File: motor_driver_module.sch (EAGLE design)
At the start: 55 parts, among them IC1 LTC6088, IC7 DRV8833RTY, IC8 DRV8833RTY, P1 BAT+, P10 MD2, P11 MA_IN1, P12 MA_IN2, P13 MB_IN1, P14 MB_IN2, P15 MC_IN1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

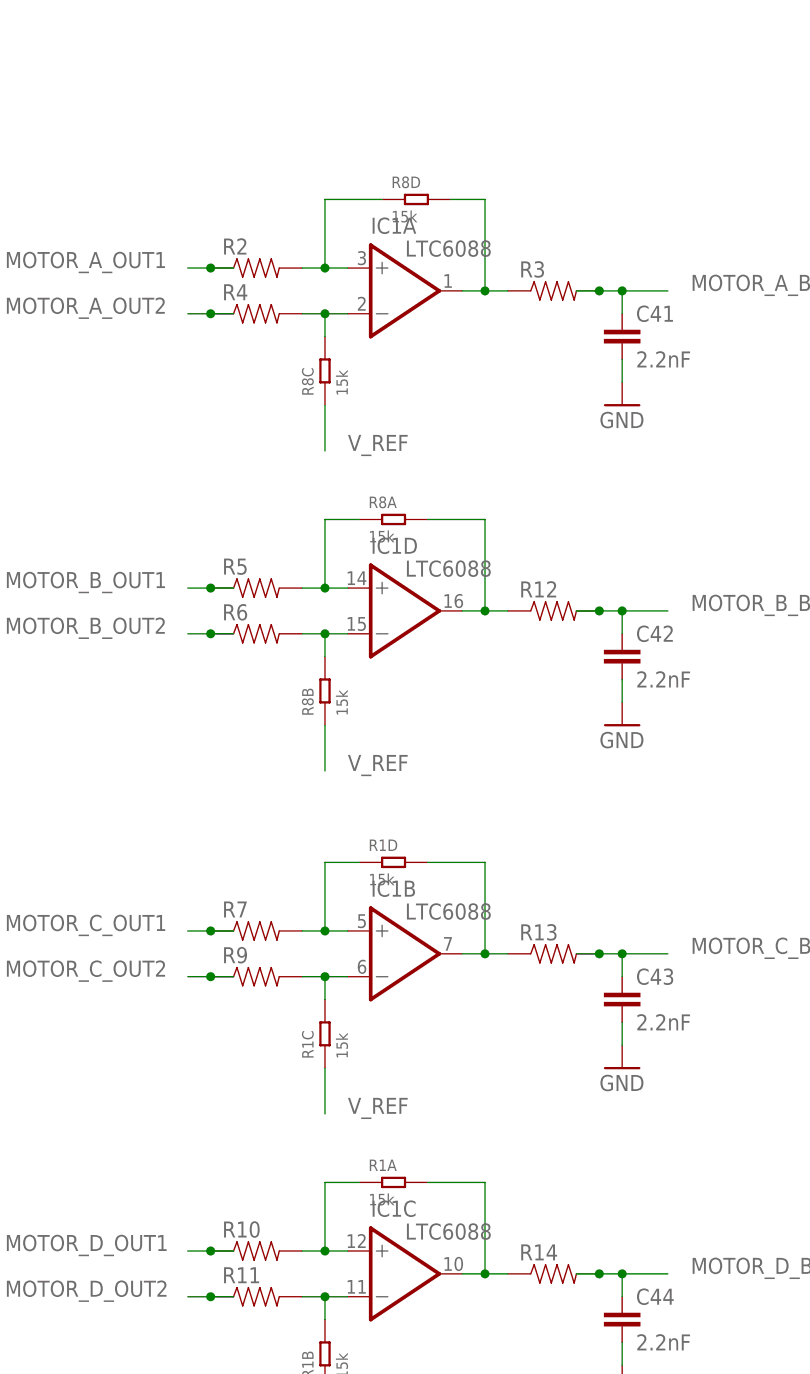
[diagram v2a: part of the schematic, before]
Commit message: More routing. No progress.
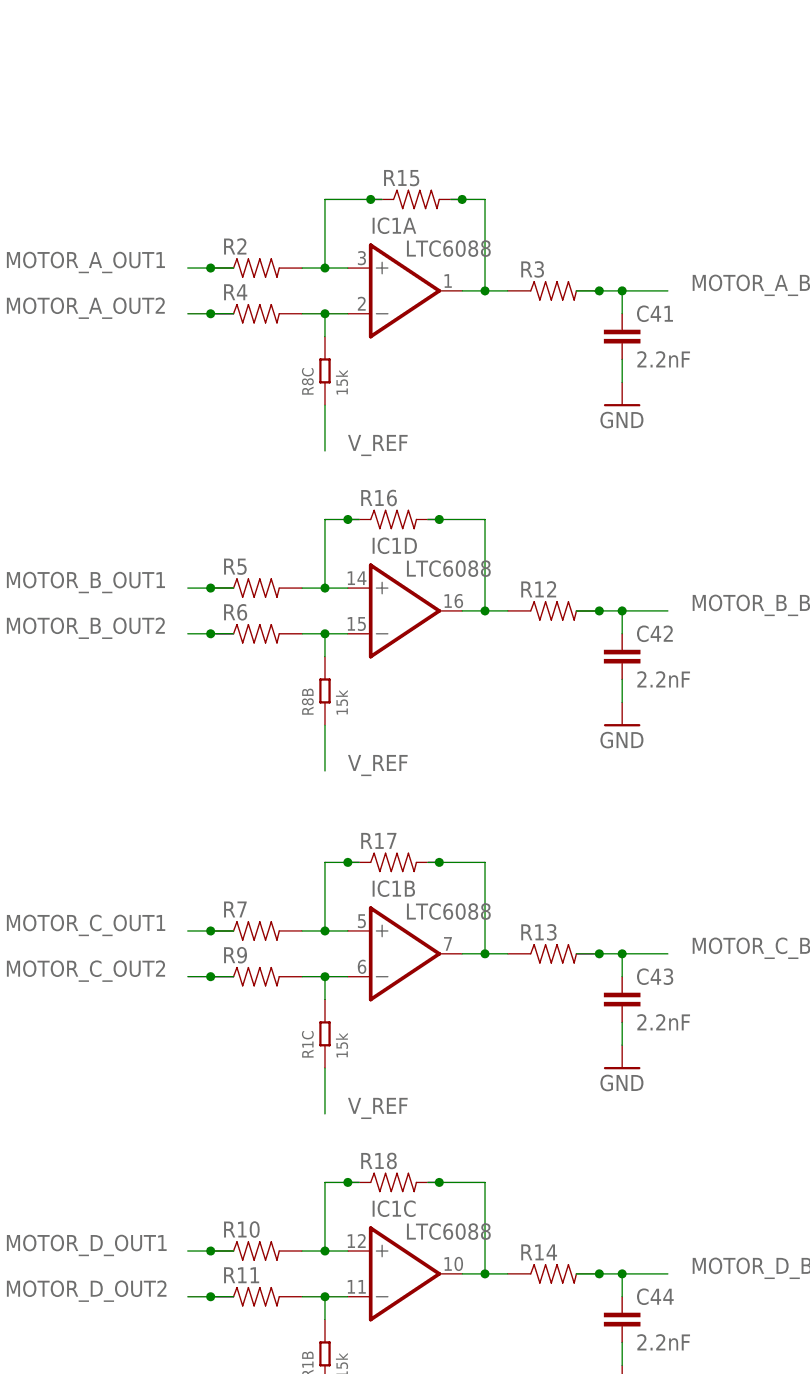
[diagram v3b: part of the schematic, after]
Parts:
- added R15, R16, R17, R18: (no value), biomimetic:RESISTOR0402-RES
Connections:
- net N$22: now also R16.1; no longer R8A.1
- net N$24: now also R17.1; no longer R1D.1
- net N$26: now also R18.1; no longer R1A.1
- net N$30: now also R15.1; no longer R8D.1
- net N$34: now also R18.2; no longer R1A.2
- net N$35: now also R17.2; no longer R1D.2
- net N$36: now also R15.2; no longer R8D.2
- net N$37: now also R16.2; no longer R8A.2
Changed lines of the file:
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@@
 <part name="R13" library="biomimetic" deviceset="RESISTOR" device="0402-RES"/>
 <part name="R14" library="biomimetic" deviceset="RESISTOR" device="0402-RES"/>
+<part name="R15" library="biomimetic" deviceset="RESISTOR" device="0402-RES"/>
+<part name="R16" library="biomimetic" deviceset="RESISTOR" device="0402-RES"/>
+<part name="R17" library="biomimetic" deviceset="RESISTOR" device="0402-RES"/>
+<part name="R18" library="biomimetic" deviceset="RESISTOR" device="0402-RES"/>
 </parts>
 <sheets>
@@
 <attribute name="VALUE" x="276.86" y="220.98" size="1.778" layer="96"/>
 </instance>
-<instance part="R1" gate="D" x="154.94" y="104.14"/>
-<instance part="R1" gate="A" x="154.94" y="68.58"/>
-<instance part="R8" gate="D" x="157.48" y="177.8"/>
-<instance part="R8" gate="A" x="154.94" y="142.24"/>
 <instance part="R8" gate="B" x="147.32" y="123.19" rot="R90"/>
 <instance part="R1" gate="C" x="147.32" y="85.09" rot="R90"/>
@@
 <instance part="R13" gate="G$1" x="172.72" y="93.98"/>
 <instance part="R14" gate="G$1" x="172.72" y="58.42"/>
+<instance part="R15" gate="G$1" x="157.48" y="177.8"/>
+<instance part="R16" gate="G$1" x="154.94" y="142.24"/>
+<instance part="R17" gate="G$1" x="154.94" y="104.14"/>
+<instance part="R18" gate="G$1" x="154.94" y="68.58"/>
 </instances>
 <busses>
@@
 <wire x1="144.78" y1="170.18" x2="147.32" y2="170.18" width="0.1524" layer="91"/>
 <wire x1="147.32" y1="170.18" x2="147.32" y2="177.8" width="0.1524" layer="91"/>
-<wire x1="147.32" y1="177.8" x2="153.67" y2="177.8" width="0.1524" layer="91"/>
+<wire x1="147.32" y1="177.8" x2="152.4" y2="177.8" width="0.1524" layer="91"/>
+<wire x1="152.4" y1="177.8" x2="153.67" y2="177.8" width="0.1524" layer="91"/>
 <wire x1="149.86" y1="170.18" x2="147.32" y2="170.18" width="0.1524" layer="91"/>
 <junction x="147.32" y="170.18"/>
-<pinref part="R8" gate="D" pin="1"/>
 <pinref part="IC1" gate="A" pin="+IN"/>
 <pinref part="R2" gate="G$1" pin="2"/>
+<pinref part="R15" gate="G$1" pin="1"/>
+<junction x="152.4" y="177.8"/>
 </segment>
 </net>
@@
 <segment>
 <wire x1="147.32" y1="134.62" x2="147.32" y2="142.24" width="0.1524" layer="91"/>
-<wire x1="147.32" y1="142.24" x2="151.13" y2="142.24" width="0.1524" layer="91"/>
+<wire x1="147.32" y1="142.24" x2="149.86" y2="142.24" width="0.1524" layer="91"/>
+<wire x1="149.86" y1="142.24" x2="151.13" y2="142.24" width="0.1524" layer="91"/>
 <wire x1="149.86" y1="134.62" x2="147.32" y2="134.62" width="0.1524" layer="91"/>
 <wire x1="144.78" y1="134.62" x2="147.32" y2="134.62" width="0.1524" layer="91"/>
 <junction x="147.32" y="134.62"/>
-<pinref part="R8" gate="A" pin="1"/>
 <pinref part="IC1" gate="D" pin="+IN"/>
 <pinref part="R5" gate="G$1" pin="2"/>
+<pinref part="R16" gate="G$1" pin="1"/>
+<junction x="149.86" y="142.24"/>
 </segment>
 </net>
@@
 <wire x1="144.78" y1="96.52" x2="147.32" y2="96.52" width="0.1524" layer="91"/>
 <wire x1="147.32" y1="96.52" x2="147.32" y2="104.14" width="0.1524" layer="91"/>
-<wire x1="147.32" y1="104.14" x2="151.13" y2="104.14" width="0.1524" layer="91"/>
+<wire x1="147.32" y1="104.14" x2="149.86" y2="104.14" width="0.1524" layer="91"/>
+<wire x1="149.86" y1="104.14" x2="151.13" y2="104.14" width="0.1524" layer="91"/>
 <wire x1="149.86" y1="96.52" x2="147.32" y2="96.52" width="0.1524" layer="91"/>
 <junction x="147.32" y="96.52"/>
-<pinref part="R1" gate="D" pin="1"/>
 <pinref part="IC1" gate="B" pin="+IN"/>
 <pinref part="R7" gate="G$1" pin="2"/>
+<pinref part="R17" gate="G$1" pin="1"/>
+<junction x="149.86" y="104.14"/>
 </segment>
 </net>
@@
 <wire x1="144.78" y1="60.96" x2="147.32" y2="60.96" width="0.1524" layer="91"/>
 <wire x1="147.32" y1="60.96" x2="147.32" y2="68.58" width="0.1524" layer="91"/>
-<wire x1="147.32" y1="68.58" x2="151.13" y2="68.58" width="0.1524" layer="91"/>
+<wire x1="147.32" y1="68.58" x2="149.86" y2="68.58" width="0.1524" layer="91"/>
+<wire x1="149.86" y1="68.58" x2="151.13" y2="68.58" width="0.1524" layer="91"/>
 <wire x1="149.86" y1="60.96" x2="147.32" y2="60.96" width="0.1524" layer="91"/>
 <junction x="147.32" y="60.96"/>
-<pinref part="R1" gate="A" pin="1"/>
 <pinref part="IC1" gate="C" pin="+IN"/>
 <pinref part="R10" gate="G$1" pin="2"/>
+<pinref part="R18" gate="G$1" pin="1"/>
+<junction x="149.86" y="68.58"/>
 </segment>
 </net>
@@
 <segment>
 <wire x1="162.56" y1="58.42" x2="165.1" y2="58.42" width="0.1524" layer="91"/>
-<wire x1="158.75" y1="68.58" x2="165.1" y2="68.58" width="0.1524" layer="91"/>
+<wire x1="158.75" y1="68.58" x2="160.02" y2="68.58" width="0.1524" layer="91"/>
+<wire x1="160.02" y1="68.58" x2="165.1" y2="68.58" width="0.1524" layer="91"/>
 <wire x1="165.1" y1="68.58" x2="165.1" y2="58.42" width="0.1524" layer="91"/>
-<pinref part="R1" gate="A" pin="2"/>
 <wire x1="165.1" y1="58.42" x2="167.64" y2="58.42" width="0.1524" layer="91"/>
 <junction x="165.1" y="58.42"/>
 <pinref part="IC1" gate="C" pin="OUT"/>
 <pinref part="R14" gate="G$1" pin="1"/>
+<pinref part="R18" gate="G$1" pin="2"/>
+<junction x="160.02" y="68.58"/>
 </segment>
 </net>
@@
 <segment>
 <wire x1="162.56" y1="93.98" x2="165.1" y2="93.98" width="0.1524" layer="91"/>
-<wire x1="158.75" y1="104.14" x2="165.1" y2="104.14" width="0.1524" layer="91"/>
+<wire x1="158.75" y1="104.14" x2="160.02" y2="104.14" width="0.1524" layer="91"/>
+<wire x1="160.02" y1="104.14" x2="165.1" y2="104.14" width="0.1524" layer="91"/>
 <wire x1="165.1" y1="104.14" x2="165.1" y2="93.98" width="0.1524" layer="91"/>
-<pinref part="R1" gate="D" pin="2"/>
 <wire x1="165.1" y1="93.98" x2="167.64" y2="93.98" width="0.1524" layer="91"/>
 <junction x="165.1" y="93.98"/>
 <pinref part="IC1" gate="B" pin="OUT"/>
 <pinref part="R13" gate="G$1" pin="1"/>
+<pinref part="R17" gate="G$1" pin="2"/>
+<junction x="160.02" y="104.14"/>
 </segment>
 </net>
@@
 <segment>
 <wire x1="162.56" y1="132.08" x2="165.1" y2="132.08" width="0.1524" layer="91"/>
-<wire x1="158.75" y1="142.24" x2="165.1" y2="142.24" width="0.1524" layer="91"/>
+<wire x1="158.75" y1="142.24" x2="160.02" y2="142.24" width="0.1524" layer="91"/>
+<wire x1="160.02" y1="142.24" x2="165.1" y2="142.24" width="0.1524" layer="91"/>
 <wire x1="165.1" y1="142.24" x2="165.1" y2="132.08" width="0.1524" layer="91"/>
-<pinref part="R8" gate="A" pin="2"/>
 <wire x1="165.1" y1="132.08" x2="167.64" y2="132.08" width="0.1524" layer="91"/>
 <junction x="165.1" y="132.08"/>
 <pinref part="IC1" gate="D" pin="OUT"/>
 <pinref part="R12" gate="G$1" pin="1"/>
+<pinref part="R16" gate="G$1" pin="2"/>
+<junction x="160.02" y="142.24"/>
 </segment>
 </net>
@@
 <segment>
 <wire x1="162.56" y1="167.64" x2="165.1" y2="167.64" width="0.1524" layer="91"/>
-<wire x1="161.29" y1="177.8" x2="165.1" y2="177.8" width="0.1524" layer="91"/>
+<wire x1="161.29" y1="177.8" x2="162.56" y2="177.8" width="0.1524" layer="91"/>
+<wire x1="162.56" y1="177.8" x2="165.1" y2="177.8" width="0.1524" layer="91"/>
 <wire x1="165.1" y1="177.8" x2="165.1" y2="167.64" width="0.1524" layer="91"/>
-<pinref part="R8" gate="D" pin="2"/>
 <wire x1="165.1" y1="167.64" x2="167.64" y2="167.64" width="0.1524" layer="91"/>
 <junction x="165.1" y="167.64"/>
 <pinref part="IC1" gate="A" pin="OUT"/>
 <pinref part="R3" gate="G$1" pin="1"/>
-</segment>
-</net>
+<pinref part="R15" gate="G$1" pin="2"/>
+<junction x="162.56" y="177.8"/>
+</segment>
+</net>

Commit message: Further routing. No progress.
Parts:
- added R19, R20: (no value), biomimetic:RESISTOR0402-RES
- R1, R8: value 15k -> (none); device OPL Eagle Library:R-4R -> biomimetic:RESISTOR0402-RES
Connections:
- net N$22: now also IC1A.+IN; no longer IC1D.+IN
- net N$23: now also IC1A.-IN, R8.2; no longer IC1D.-IN, R8B.2
- net N$25: now also R19.2; no longer R1C.2
- net N$27: now also R20.2; no longer R1B.2
- net N$30: now also IC1D.+IN; no longer IC1A.+IN
- net N$31: now also IC1D.-IN, R1.2; no longer IC1A.-IN, R8C.2
- net N$36: now also IC1D.OUT; no longer IC1A.OUT
- net N$37: now also IC1A.OUT; no longer IC1D.OUT
- net V_REF: now also R1.1, R19.1, R20.1, R8.1; no longer R1B.1, R1C.1, R8B.1, R8C.1
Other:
- moved on the sheet: IC1A, IC1D
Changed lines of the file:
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@@
 <part name="GND33" library="biomimetic" deviceset="GND" device=""/>
 <part name="GND46" library="biomimetic" deviceset="GND" device=""/>
-<part name="R8" library="OPL Eagle Library" deviceset="R-4R*" device="" value="15k"/>
 <part name="C47" library="biomimetic" deviceset="CAP" device="0402-CAP" value="0.1uF"/>
 <part name="U$1" library="biomimetic" deviceset="3.3V" device=""/>
@@
 <part name="P21" library="wirepad" deviceset="SMD2" device="" value="MOTOR_C_BEMF"/>
 <part name="P22" library="wirepad" deviceset="SMD2" device="" value="MOTOR_D_BEMF"/>
-<part name="R1" library="OPL Eagle Library" deviceset="R-4R*" device="" value="15k"/>
 <part name="IC1" library="biomimetic" deviceset="LTC6088" device=""/>
 <part name="R2" library="biomimetic" deviceset="RESISTOR" device="0402-RES"/>
@@
 <part name="R17" library="biomimetic" deviceset="RESISTOR" device="0402-RES"/>
 <part name="R18" library="biomimetic" deviceset="RESISTOR" device="0402-RES"/>
+<part name="R1" library="biomimetic" deviceset="RESISTOR" device="0402-RES"/>
+<part name="R8" library="biomimetic" deviceset="RESISTOR" device="0402-RES"/>
+<part name="R19" library="biomimetic" deviceset="RESISTOR" device="0402-RES"/>
+<part name="R20" library="biomimetic" deviceset="RESISTOR" device="0402-RES"/>
 </parts>
 <sheets>
@@
 <instance part="U$1" gate="G$1" x="111.76" y="30.48"/>
 <instance part="GND24" gate="1" x="111.76" y="7.62"/>
-<instance part="R8" gate="C" x="147.32" y="158.75" rot="R90"/>
 <instance part="P3" gate="1" x="304.8" y="160.02" smashed="yes">
 <attribute name="NAME" x="289.56" y="160.02" size="1.778" layer="95"/>
@@
 <attribute name="VALUE" x="276.86" y="220.98" size="1.778" layer="96"/>
 </instance>
-<instance part="R8" gate="B" x="147.32" y="123.19" rot="R90"/>
-<instance part="R1" gate="C" x="147.32" y="85.09" rot="R90"/>
-<instance part="R1" gate="B" x="147.32" y="49.53" rot="R90"/>
-<instance part="IC1" gate="A" x="154.94" y="167.64"/>
 <instance part="IC1" gate="B" x="154.94" y="93.98"/>
 <instance part="IC1" gate="C" x="154.94" y="58.42"/>
-<instance part="IC1" gate="D" x="154.94" y="132.08"/>
 <instance part="IC1" gate="P" x="111.76" y="20.32"/>
 <instance part="R2" gate="G$1" x="139.7" y="170.18"/>
@@
 <instance part="R17" gate="G$1" x="154.94" y="104.14"/>
 <instance part="R18" gate="G$1" x="154.94" y="68.58"/>
+<instance part="IC1" gate="D" x="154.94" y="167.64"/>
+<instance part="IC1" gate="A" x="154.94" y="132.08"/>
+<instance part="R1" gate="G$1" x="147.32" y="157.48" rot="R90"/>
+<instance part="R8" gate="G$1" x="147.32" y="121.92" rot="R90"/>
+<instance part="R19" gate="G$1" x="147.32" y="83.82" rot="R90"/>
+<instance part="R20" gate="G$1" x="147.32" y="48.26" rot="R90"/>
 </instances>
 <busses>
@@
 <wire x1="149.86" y1="170.18" x2="147.32" y2="170.18" width="0.1524" layer="91"/>
 <junction x="147.32" y="170.18"/>
-<pinref part="IC1" gate="A" pin="+IN"/>
 <pinref part="R2" gate="G$1" pin="2"/>
 <pinref part="R15" gate="G$1" pin="1"/>
 <junction x="152.4" y="177.8"/>
+<pinref part="IC1" gate="D" pin="+IN"/>
 </segment>
 </net>
@@
 <wire x1="149.86" y1="165.1" x2="147.32" y2="165.1" width="0.1524" layer="91"/>
 <junction x="147.32" y="165.1"/>
-<pinref part="R8" gate="C" pin="2"/>
-<pinref part="IC1" gate="A" pin="-IN"/>
 <pinref part="R4" gate="G$1" pin="2"/>
+<pinref part="IC1" gate="D" pin="-IN"/>
+<pinref part="R1" gate="G$1" pin="2"/>
 </segment>
 </net>
@@
 <wire x1="144.78" y1="134.62" x2="147.32" y2="134.62" width="0.1524" layer="91"/>
 <junction x="147.32" y="134.62"/>
-<pinref part="IC1" gate="D" pin="+IN"/>
 <pinref part="R5" gate="G$1" pin="2"/>
 <pinref part="R16" gate="G$1" pin="1"/>
 <junction x="149.86" y="142.24"/>
+<pinref part="IC1" gate="A" pin="+IN"/>
 </segment>
 </net>
@@
 <wire x1="144.78" y1="129.54" x2="147.32" y2="129.54" width="0.1524" layer="91"/>
 <junction x="147.32" y="129.54"/>
-<pinref part="R8" gate="B" pin="2"/>
-<pinref part="IC1" gate="D" pin="-IN"/>
 <pinref part="R6" gate="G$1" pin="2"/>
+<pinref part="IC1" gate="A" pin="-IN"/>
+<pinref part="R8" gate="G$1" pin="2"/>
 </segment>
 </net>
@@
 <wire x1="149.86" y1="91.44" x2="147.32" y2="91.44" width="0.1524" layer="91"/>
 <junction x="147.32" y="91.44"/>
-<pinref part="R1" gate="C" pin="2"/>
 <pinref part="IC1" gate="B" pin="-IN"/>
 <pinref part="R9" gate="G$1" pin="2"/>
+<pinref part="R19" gate="G$1" pin="2"/>
 </segment>
 </net>
@@
 <wire x1="149.86" y1="55.88" x2="147.32" y2="55.88" width="0.1524" layer="91"/>
 <junction x="147.32" y="55.88"/>
-<pinref part="R1" gate="B" pin="2"/>
 <pinref part="IC1" gate="C" pin="-IN"/>
 <pinref part="R11" gate="G$1" pin="2"/>
+<pinref part="R20" gate="G$1" pin="2"/>
 </segment>
 </net>
@@
 </segment>
 <segment>
-<wire x1="147.32" y1="149.86" x2="147.32" y2="154.94" width="0.1524" layer="91"/>
+<wire x1="147.32" y1="149.86" x2="147.32" y2="152.4" width="0.1524" layer="91"/>
 <label x="149.86" y="149.86" size="1.778" layer="95"/>
-<pinref part="R8" gate="C" pin="1"/>
-</segment>
-<segment>
-<wire x1="147.32" y1="114.3" x2="147.32" y2="119.38" width="0.1524" layer="91"/>
+<pinref part="R1" gate="G$1" pin="1"/>
+<wire x1="147.32" y1="152.4" x2="147.32" y2="154.94" width="0.1524" layer="91"/>
+<junction x="147.32" y="152.4"/>
+</segment>
+<segment>
+<wire x1="147.32" y1="114.3" x2="147.32" y2="116.84" width="0.1524" layer="91"/>
 <label x="149.86" y="114.3" size="1.778" layer="95"/>
-<pinref part="R8" gate="B" pin="1"/>
+<pinref part="R8" gate="G$1" pin="1"/>
+<wire x1="147.32" y1="116.84" x2="147.32" y2="119.38" width="0.1524" layer="91"/>
+<junction x="147.32" y="116.84"/>
 </segment>
 <segment>
 <label x="149.86" y="76.2" size="1.778" layer="95"/>
-<wire x1="147.32" y1="76.2" x2="147.32" y2="81.28" width="0.1524" layer="91"/>
-<pinref part="R1" gate="C" pin="1"/>
+<wire x1="147.32" y1="76.2" x2="147.32" y2="78.74" width="0.1524" layer="91"/>
+<pinref part="R19" gate="G$1" pin="1"/>
+<wire x1="147.32" y1="78.74" x2="147.32" y2="81.28" width="0.1524" layer="91"/>
+<junction x="147.32" y="78.74"/>
 </segment>
 <segment>
 <label x="149.86" y="40.64" size="1.778" layer="95"/>
-<wire x1="147.32" y1="40.64" x2="147.32" y2="45.72" width="0.1524" layer="91"/>
-<pinref part="R1" gate="B" pin="1"/>
+<wire x1="147.32" y1="40.64" x2="147.32" y2="43.18" width="0.1524" layer="91"/>
+<pinref part="R20" gate="G$1" pin="1"/>
+<wire x1="147.32" y1="43.18" x2="147.32" y2="45.72" width="0.1524" layer="91"/>
+<junction x="147.32" y="43.18"/>
 </segment>
 </net>
@@
 <wire x1="165.1" y1="132.08" x2="167.64" y2="132.08" width="0.1524" layer="91"/>
 <junction x="165.1" y="132.08"/>
-<pinref part="IC1" gate="D" pin="OUT"/>
 <pinref part="R12" gate="G$1" pin="1"/>
 <pinref part="R16" gate="G$1" pin="2"/>
 <junction x="160.02" y="142.24"/>
+<pinref part="IC1" gate="A" pin="OUT"/>
 </segment>
 </net>
@@
 <wire x1="165.1" y1="167.64" x2="167.64" y2="167.64" width="0.1524" layer="91"/>
 <junction x="165.1" y="167.64"/>
-<pinref part="IC1" gate="A" pin="OUT"/>
 <pinref part="R3" gate="G$1" pin="1"/>
 <pinref part="R15" gate="G$1" pin="2"/>
 <junction x="162.56" y="177.8"/>
-</segment>
-</net>
+<pinref part="IC1" gate="D" pin="OUT"/>
+</segment>
+</net>
